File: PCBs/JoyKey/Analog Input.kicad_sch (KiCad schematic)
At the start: 3 parts, among them SW1 RotaryEncoder_Switch, SW14 SW_Push_45deg, U2 2_axis_pot_joystick

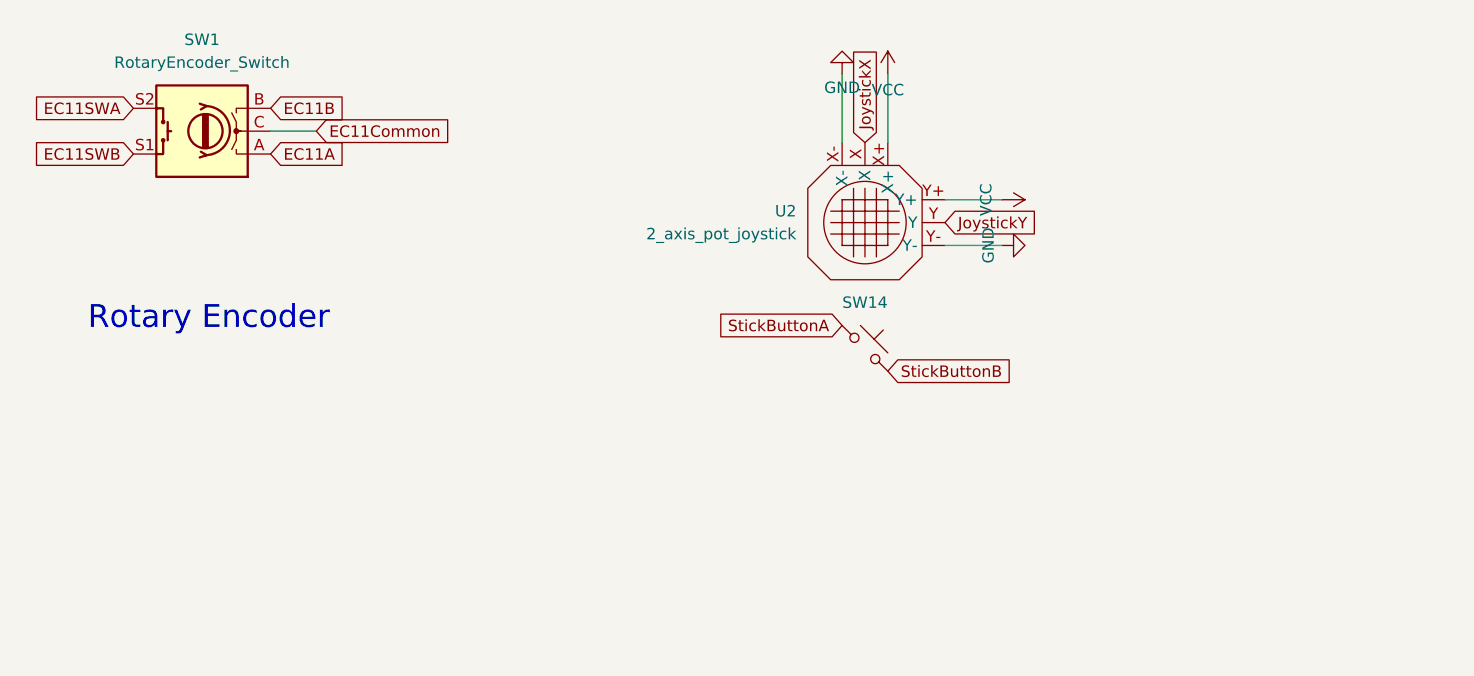
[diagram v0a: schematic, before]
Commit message: Simplified analog input schematic and added proper joystick symbol
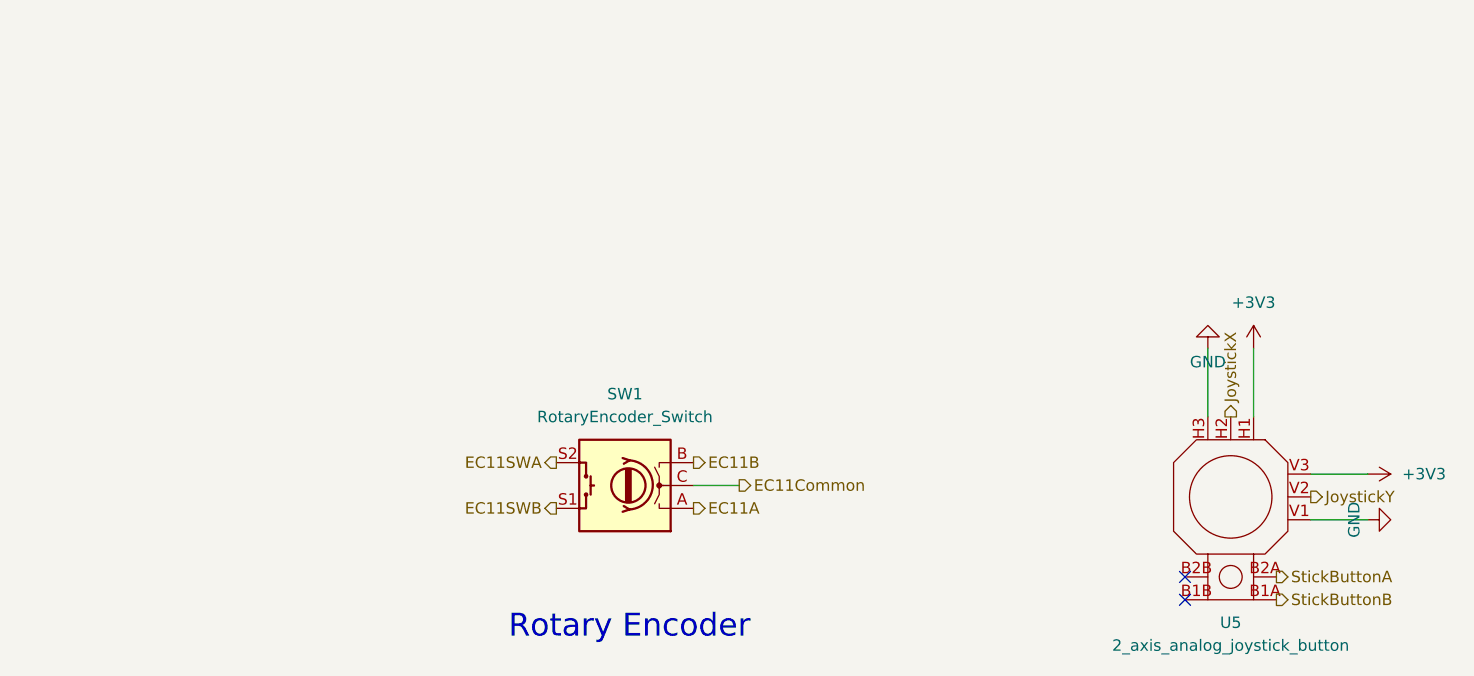
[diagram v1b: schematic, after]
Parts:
- removed SW14: SW_Push_45deg, MX_Solderable:MX-Solderable-1U, symbol Switch:SW_Push_45deg
- removed U2: 2_axis_pot_joystick, symbol custom_Interface_HID:2_axis_pot_joystick
- added U5: 2_axis_analog_joystick_button, custom_Interface_HID:Adafruit 2-Axis joystick, symbol custom_Interface_HID:2_axis_analog_joystick_button
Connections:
- net GND: now also U5.H3, U5.V1
- net JoystickX: now also U5.H2
- net JoystickY: now also U5.V2
- net StickButtonA: now also U5.B2A
- net StickButtonB: now also U5.B1A
- new net +3V3: U5.H1, U5.V3
- no-connect marks 0 -> 2
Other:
- moved on the sheet: SW1

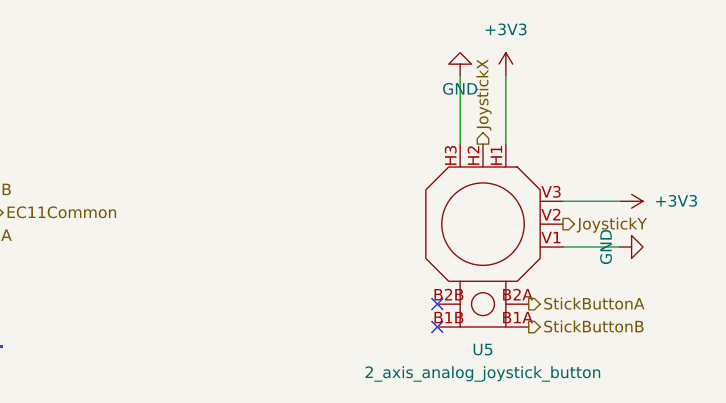
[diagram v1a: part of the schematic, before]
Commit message: Added Mating Point to joystick schematic
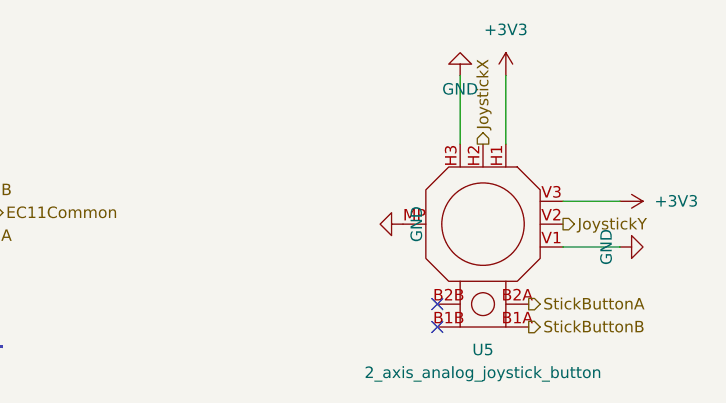
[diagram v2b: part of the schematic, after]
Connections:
- net GND: now also U5.MP
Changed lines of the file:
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@@
 		(pin "V1"
+		)
+		(pin "MP"
 		)
 		(instances
@@
 					(unit 1)
 				)
+			)
+		)
+	)
+	(symbol
+		(lib_id "power:GND")
+		(at 172.72 88.9 270)
+		(unit 1)
+		(exclude_from_sim no)
+		(in_bom yes)
+		(on_board yes)
+		(dnp no)
+		(property "Reference" "#PWR011"
+			(at 166.37 88.9 0)
+			(effects
+				(font
+					(size 1.27 1.27)
+				)
+				(hide yes)
+			)
+		)
+		(property "Value" "GND"
+			(at 174.244 88.9 0)
+			(effects
+				(font
+					(size 1.27 1.27)
+				)
+			)
+		)
+		(property "Footprint" ""
+			(at 172.72 88.9 0)
+			(effects
+				(font
+					(size 1.27 1.27)
+				)
+				(hide yes)
+			)
+		)
+		(property "Datasheet" ""
+			(at 172.72 88.9 0)
+			(effects
+				(font
+					(size 1.27 1.27)
+				)
+				(hide yes)
+			)
+		)
+		(property "Description" "Power symbol creates a global label with name \"GND\" , ground"
+			(at 172.72 88.9 0)
+			(effects
+				(font
+					(size 1.27 1.27)
+				)
+				(hide yes)
+			)
+		)
+		(pin "1"
+		)
+		(instances
+			(project "JoyKey"
+				(path "/7995ec7a-c14b-437e-b354-3eb74052b7cb/a78c392f-6f7c-48a6-aa3f-986a350bb68a"
+					(reference "#PWR011")
+					(unit 1)
+				)

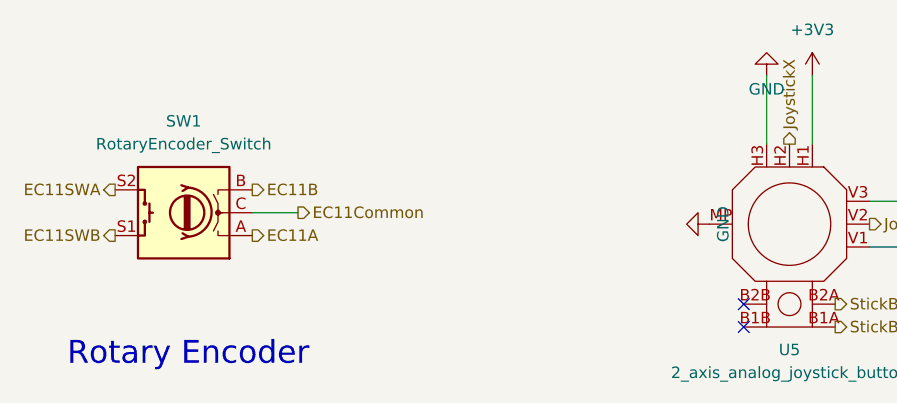
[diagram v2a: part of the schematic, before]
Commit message: Add Mating point GND to encoder
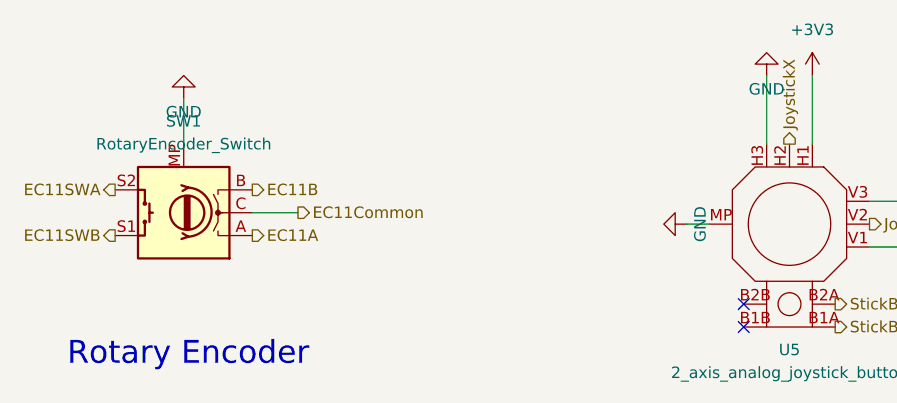
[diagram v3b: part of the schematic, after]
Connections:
- net GND: now also SW1.MP
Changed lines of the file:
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@@
+	(wire
+		(pts
+			(xy 170.18 88.9) (xy 172.72 88.9)
+		)
+		(stroke
+			(width 0)
+			(type default)
+		)
+	)
 	(wire
 		(pts
@@
 		(pts
 			(xy 184.15 72.39) (xy 184.15 80.01)
+		)
+		(stroke
+			(width 0)
+			(type default)
+		)
+	)
+	(wire
+		(pts
+			(xy 114.3 74.93) (xy 114.3 80.01)
 		)
 		(stroke
@@
 	(symbol
 		(lib_id "power:GND")
-		(at 172.72 88.9 270)
+		(at 170.18 88.9 270)
 		(unit 1)
 		(exclude_from_sim no)
@@
 		(dnp no)
 		(property "Reference" "#PWR011"
-			(at 166.37 88.9 0)
+			(at 163.83 88.9 0)
 			(effects
 				(font
@@
 		)
 		(property "Value" "GND"
-			(at 174.244 88.9 0)
+			(at 171.704 88.9 0)
 			(effects
 				(font
@@
 		)
 		(property "Footprint" ""
-			(at 172.72 88.9 0)
+			(at 170.18 88.9 0)
 			(effects
 				(font
@@
 		)
 		(property "Datasheet" ""
-			(at 172.72 88.9 0)
+			(at 170.18 88.9 0)
 			(effects
 				(font
@@
 		)
 		(property "Description" "Power symbol creates a global label with name \"GND\" , ground"
-			(at 172.72 88.9 0)
+			(at 170.18 88.9 0)
 			(effects
 				(font
@@
 		(pin "C"
 		)
+		(pin "MP"
+		)
 		(instances
 			(project "JoyKey"
@@
 					(unit 1)
 				)
+			)
+		)
+	)
+	(symbol
+		(lib_id "power:GND")
+		(at 114.3 74.93 180)
+		(unit 1)
+		(exclude_from_sim no)
+		(in_bom yes)
+		(on_board yes)
+		(dnp no)
+		(property "Reference" "#PWR012"
+			(at 114.3 68.58 0)
+			(effects
+				(font
+					(size 1.27 1.27)
+				)
+				(hide yes)
+			)
+		)
+		(property "Value" "GND"
+			(at 114.3 76.454 0)
+			(effects
+				(font
+					(size 1.27 1.27)
+				)
+			)
+		)
+		(property "Footprint" ""
+			(at 114.3 74.93 0)
+			(effects
+				(font
+					(size 1.27 1.27)
+				)
+				(hide yes)
+			)
+		)
+		(property "Datasheet" ""
+			(at 114.3 74.93 0)
+			(effects
+				(font
+					(size 1.27 1.27)
+				)
+				(hide yes)
+			)
+		)
+		(property "Description" "Power symbol creates a global label with name \"GND\" , ground"
+			(at 114.3 74.93 0)
+			(effects
+				(font
+					(size 1.27 1.27)
+				)
+				(hide yes)
+			)
+		)
+		(pin "1"
+		)
+		(instances
+			(project "JoyKey"
+				(path "/7995ec7a-c14b-437e-b354-3eb74052b7cb/a78c392f-6f7c-48a6-aa3f-986a350bb68a"
+					(reference "#PWR012")
+					(unit 1)
+				)

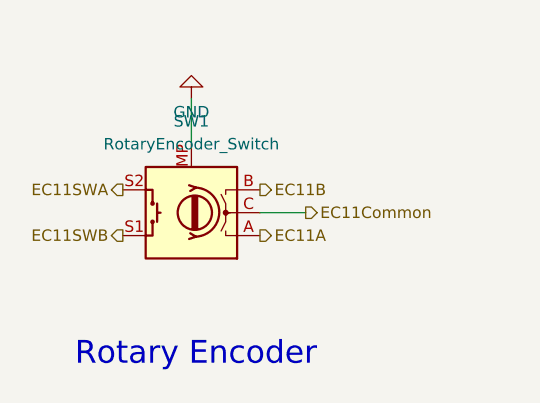
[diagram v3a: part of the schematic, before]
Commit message: Switched encoder to Alps EC12
I wanted something shorter and that didn't have a metal screw post. I do loose out on the switch though, which I've exposed via a separate header
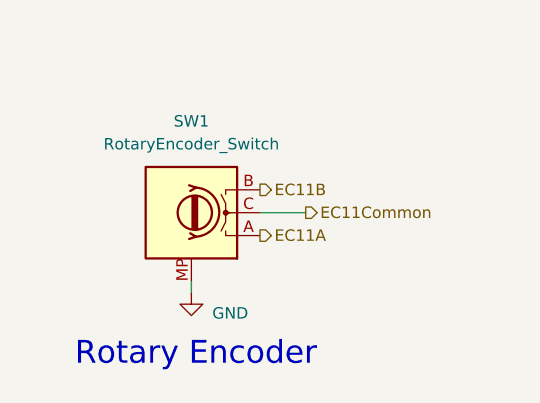
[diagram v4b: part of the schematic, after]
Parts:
- SW1: footprint Rotary_Encoder:RotaryEncoder_Alps_EC11E-Switch_Vertical_H20mm -> Rotary_Encoder:RotaryEncoder_Alps_EC12E_Vertical_H20mm; symbol Device:RotaryEncoder_Switch -> Device:RotaryEncoder
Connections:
- removed net EC11SWA: SW1.S2
- removed net EC11SWB: SW1.S1
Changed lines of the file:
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@@
 	(wire
 		(pts
-			(xy 114.3 74.93) (xy 114.3 80.01)
+			(xy 114.3 96.52) (xy 114.3 95.25)
 		)
 		(stroke
@@
 		)
 	)
-	(hierarchical_label "EC11SWA"
-		(shape output)
-		(at 106.68 85.09 180)
-		(effects
-			(font
-				(size 1.27 1.27)
-			)
-			(justify right)
-		)
-	)
 	(hierarchical_label "StickButtonB"
 		(shape output)
@@
 			)
 			(justify left)
-		)
-	)
-	(hierarchical_label "EC11SWB"
-		(shape output)
-		(at 106.68 90.17 180)
-		(effects
-			(font
-				(size 1.27 1.27)
-			)
-			(justify right)
 		)
 	)
@@
 	)
 	(symbol
-		(lib_id "Device:RotaryEncoder_Switch")
+		(lib_id "Device:RotaryEncoder")
 		(at 114.3 87.63 180)
 		(unit 1)
@@
 			)
 		)
-		(property "Footprint" "Rotary_Encoder:RotaryEncoder_Alps_EC11E-Switch_Vertical_H20mm"
+		(property "Footprint" "Rotary_Encoder:RotaryEncoder_Alps_EC12E_Vertical_H20mm"
 			(at 118.11 91.694 0)
 			(effects
@@
 			)
 		)
-		(property "Description" "Rotary encoder, dual channel, incremental quadrate outputs, with switch"
+		(property "Description" "Rotary encoder, dual channel, incremental quadrate outputs"
 			(at 114.3 87.63 0)
 			(effects
@@
 		(pin "A"
 		)
-		(pin "S1"
-		)
 		(pin "B"
-		)
-		(pin "S2"
 		)
 		(pin "C"
@@
 	(symbol
 		(lib_id "power:GND")
-		(at 114.3 74.93 180)
+		(at 114.3 96.52 0)
 		(unit 1)
 		(exclude_from_sim no)
@@
 		(dnp no)
 		(property "Reference" "#PWR012"
-			(at 114.3 68.58 0)
+			(at 114.3 102.87 0)
 			(effects
 				(font
@@
 		)
 		(property "Value" "GND"
-			(at 114.3 76.454 0)
+			(at 118.618 98.806 0)
 			(effects
 				(font
@@
 		)
 		(property "Footprint" ""
-			(at 114.3 74.93 0)
+			(at 114.3 96.52 0)
 			(effects
 				(font
@@
 		)
 		(property "Datasheet" ""
-			(at 114.3 74.93 0)
+			(at 114.3 96.52 0)
 			(effects
 				(font
@@
 		)
 		(property "Description" "Power symbol creates a global label with name \"GND\" , ground"
-			(at 114.3 74.93 0)
-			(effects
-				(font
+			(at 114.3 96.52 0)
+			(effects
+				(font
